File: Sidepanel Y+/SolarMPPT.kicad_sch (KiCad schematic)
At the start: 40 parts

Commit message: small adjustments
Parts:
- R21, R22: value tbd -> 330k
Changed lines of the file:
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@@
       (effects (font (size 1.27 1.27)) (justify right))
     )
-    (property "Value" "tbd" (id 1) (at 179.07 62.2299 0)
+    (property "Value" "330k" (id 1) (at 179.07 62.2299 0)
       (effects (font (size 1.27 1.27)) (justify right))
     )
@@
       (effects (font (size 1.27 1.27)) (justify right))
     )
-    (property "Value" "tbd" (id 1) (at 179.07 129.5399 0)
-      (effects (font (size 1.27 1.27)) (justify right))
-    )
+    (property "Value" "330k" (id 1) (at 179.07 129.5399 0)
+      (effects (font (size 1.27 1.27)) (justify right))
+    )

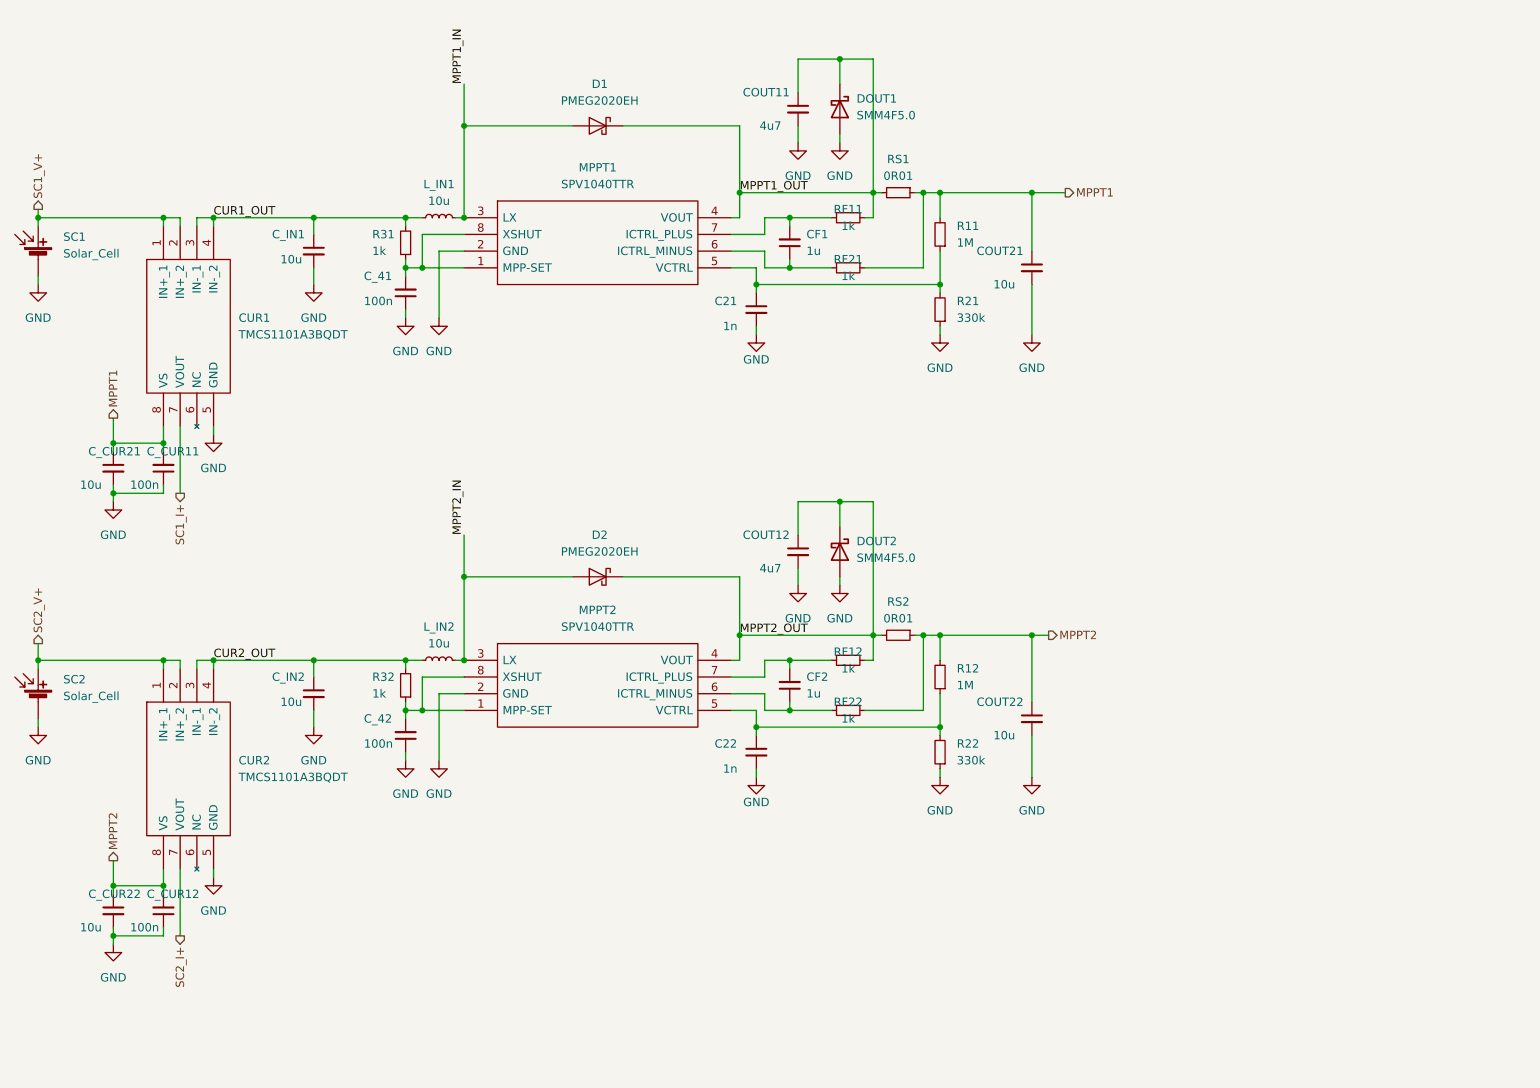
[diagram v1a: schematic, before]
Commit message: changes to the solar cell footprint + added alternative current sensing solution
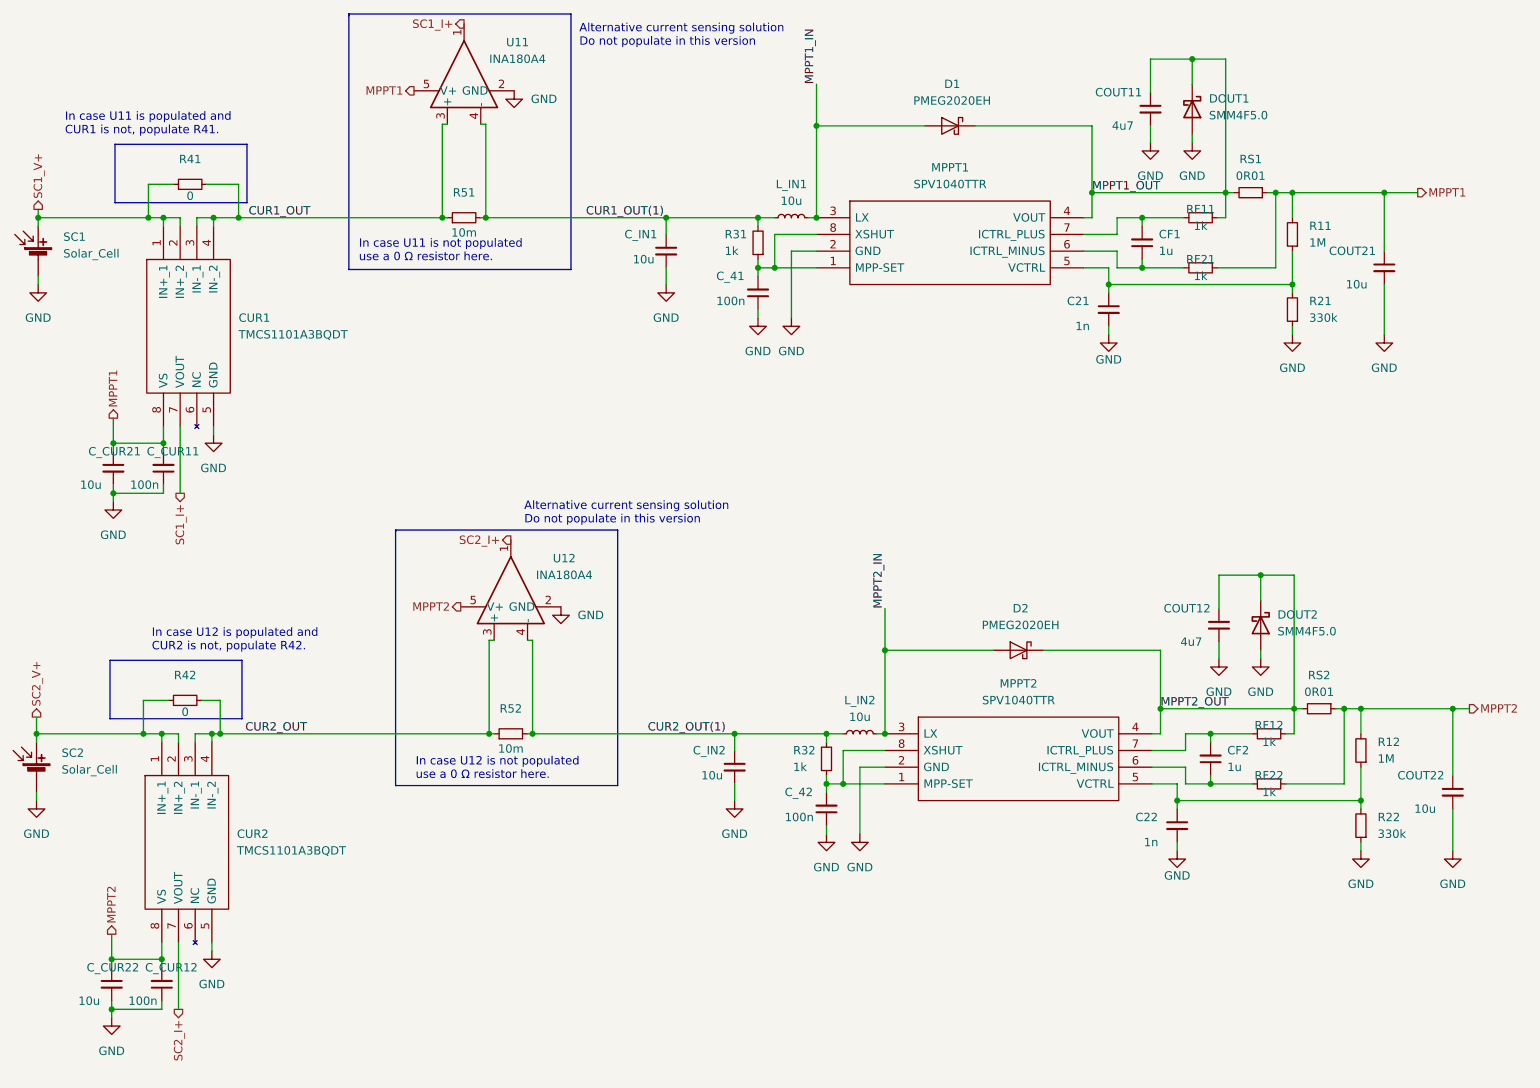
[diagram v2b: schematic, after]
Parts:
- added R41, R42: 0, Resistor_SMD:R_0603_1608Metric, symbol Device:R_Small
- added R51, R52: 10m, Resistor_SMD:R_0603_1608Metric, symbol Device:R_Small
- added U11, U12: INA180A4, Package_TO_SOT_SMD:SOT-23-5, symbol Amplifier_Current:INA180A4
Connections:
- net CUR1_OUT: now also R41.2, R51.1, U11.3 (+); no longer C_IN1.1, L_IN1.1, R31.2
- net CUR2_OUT: now also R42.2, R52.1, U12.3 (+); no longer C_IN2.1, L_IN2.1, R32.2
- net GND: now also U11.2 (GND), U12.2 (GND)
- net MPPT1: now also U11.5 (V+)
- net MPPT2: now also U12.5 (V+)
- net SC1_I+: now also U11.1
- net SC1_V+: now also R41.1
- net SC2_I+: now also U12.1
- net SC2_V+: now also R42.1
- new net CUR1_OUT(1): C_IN1.1, L_IN1.1, R31.2, R51.2, U11.4 (-)
- new net CUR2_OUT(1): C_IN2.1, L_IN2.1, R32.2, R52.2, U12.4 (-)
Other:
- note added: "Alternative current sensing solution Do not populate in this version"
- note added: "In case U11 is not populated use a 0 Ω resistor here."
- note added: "In case U11 is populated and CUR1 is not, populate R41."
- note added: "In case U12 is not populated use a 0 Ω resistor here."
- note added: "In case U12 is populated and CUR2 is not, populate R42."
- moved on the sheet: C21, C22, CF1, CF2, COUT11, COUT12, COUT21, COUT22, CUR2, C_41, C_42, C_CUR12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

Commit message: added the libraries for the specific components
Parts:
- SC1: footprint STS_Solarcells:3G30A_40x80 -> STS_solder:3G30A_40x80_Y_SC1
- SC2: footprint STS_Solarcells:3G30A_40x80 -> STS_solder:3G30A_40x80_Y_SC2
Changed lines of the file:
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@@
       (effects (font (size 1.27 1.27)) (justify left))
     )
-    (property "Footprint" "STS_Solarcells:3G30A_40x80" (id 2) (at 39.116 130.302 90)
+    (property "Footprint" "STS_solder:3G30A_40x80_Y_SC2" (id 2) (at 39.116 130.302 90)
       (effects (font (size 1.27 1.27)) hide)
     )
@@
       (effects (font (size 1.27 1.27)) (justify left))
     )
-    (property "Footprint" "STS_Solarcells:3G30A_40x80" (id 2) (at 39.37 51.816 90)
-      (effects (font (size 1.27 1.27)) hide)
-    )
+    (property "Footprint" "STS_solder:3G30A_40x80_Y_SC1" (id 2) (at 39.37 51.816 90)
+      (effects (font (size 1.27 1.27)) hide)
+    )
